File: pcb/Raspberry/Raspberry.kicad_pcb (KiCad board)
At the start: 2 copper layers, 66.4 x 48.1 mm, 26 parts, among them J1 +5V, J10 SWCLK, J11 GND, J12 SWDIO, J13 UART_TX, J14 UART_RX, J15 PC1, J16 PC0, J17 PB14, J18 GND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

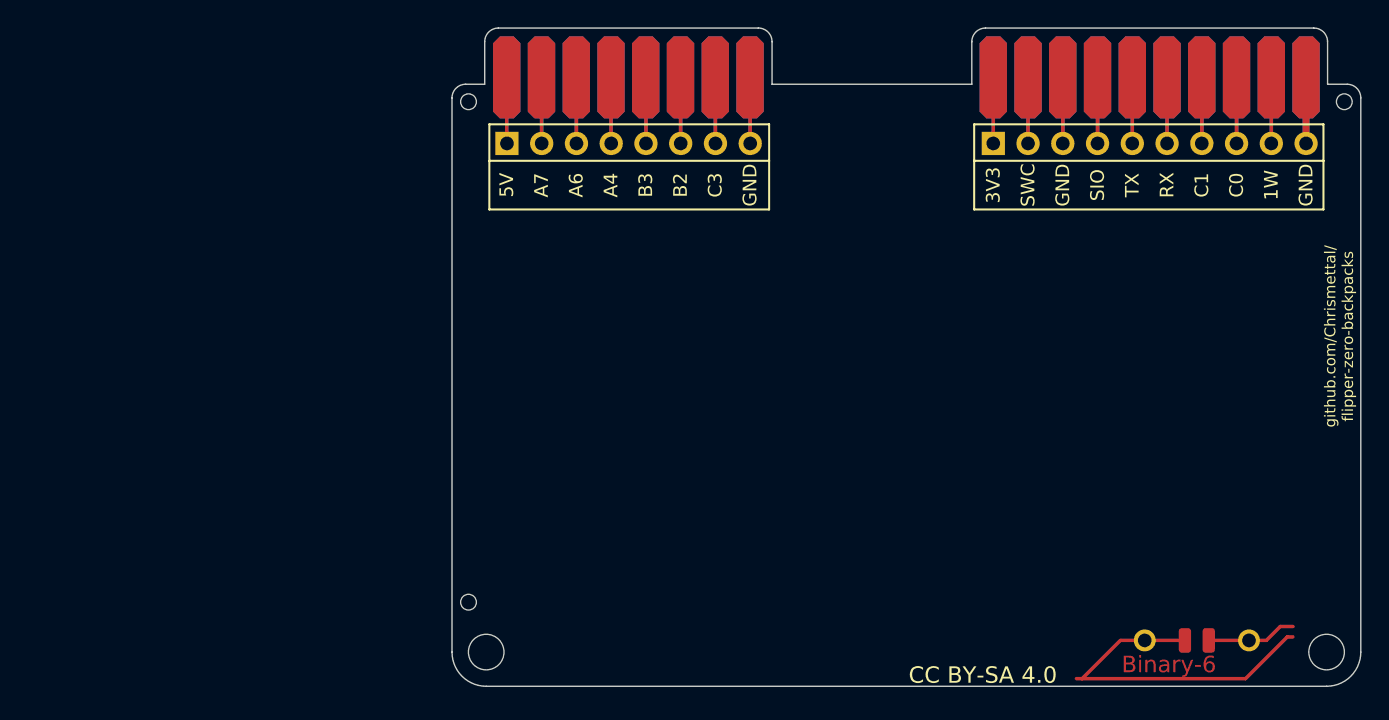
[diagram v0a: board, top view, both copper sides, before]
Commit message: [RPI] Draw schematic
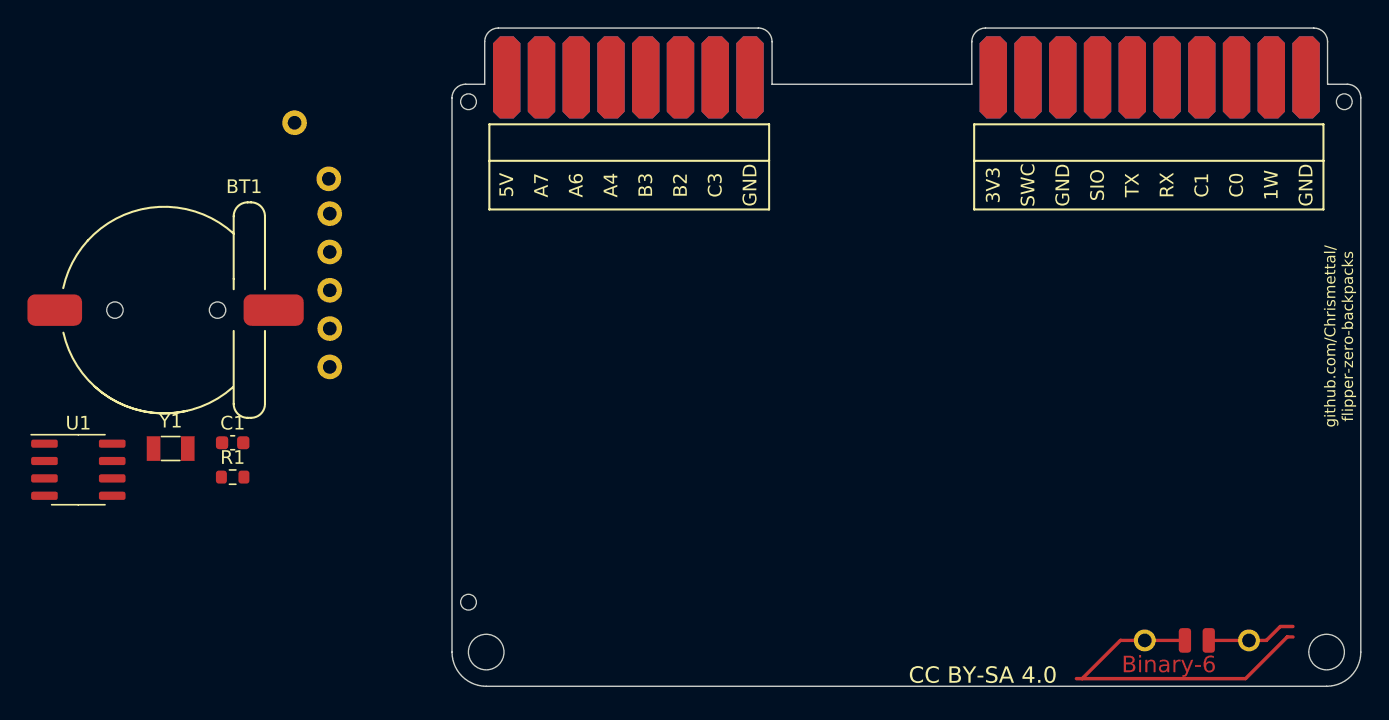
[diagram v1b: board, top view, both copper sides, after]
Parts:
- added BT1: CR1220, MeineBib:Q&J CR1220-2, F.Cu at (78.5, 104.2)
- added C1: 2.2µF, Capacitor_SMD:C_0603_1608Metric, F.Cu at (83.5, 113.9)
- added J19: +5V, MeineBib:Protopin_Small, F.Cu at (90.6, 97.1)
- added J22: FplRX_RpiTX, MeineBib:Protopin_Small, F.Cu at (90.6, 99.9)
- added J23: FlpTX_RpiRX, MeineBib:Protopin_Small, F.Cu at (90.6, 102.7)
- added J24: SCL, MeineBib:Protopin_Small, F.Cu at (90.6, 105.5)
- added J25: SDA, MeineBib:Protopin_Small, F.Cu at (90.6, 108.3)
- added R1: 1K, Resistor_SMD:R_0603_1608Metric, F.Cu at (83.5, 116.4)
- added U1: PCF8523T, Package_SO:SOIC-8_3.9x4.9mm_P1.27mm, F.Cu at (72.2, 115.9)
- added Y1: 32.768kHz, Crystal:Crystal_SMD_3215-2Pin_3.2x1.5mm, F.Cu at (78.9, 114.3)
- J20: value Conn_01x10 -> +3V3; footprint Connector_PinHeader_2.54mm:PinHeader_1x10_P2.54mm_Vertical -> MeineBib:Protopin_Small
- J21: value Conn_01x08 -> Gnd; footprint Connector_PinHeader_2.54mm:PinHeader_1x08_P2.54mm_Vertical -> MeineBib:Protopin_Small
- moved J20 48.6 mm to (90.5, 94.6)
- moved J21 15.6 mm to (88.0, 90.5)
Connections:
- J1 pad 1: Ext_+5V -> Net-(J1-Pin_1)
- J10 pad 1: Net-(J10-Pin_1) -> unconnected-(J10-Pin_1-Pad1)
- J11 pad 1: GND -> unconnected-(J11-Pin_1-Pad1)
- J12 pad 1: Net-(J12-Pin_1) -> unconnected-(J12-Pin_1-Pad1)
- J15 pad 1: Net-(J15-Pin_1) -> unconnected-(J15-Pin_1-Pad1)
- J16 pad 1: Net-(J16-Pin_1) -> unconnected-(J16-Pin_1-Pad1)
- J17 pad 1: Net-(J17-Pin_1) -> unconnected-(J17-Pin_1-Pad1)
- J2 pad 1: Net-(J2-Pin_1) -> unconnected-(J2-Pin_1-Pad1)
- J20 pad 1: Ext_+3.3V -> Net-(J20-Pin_1)
- J21 pad 1: Ext_+5V -> GND
- J3 pad 1: Net-(J21-Pin_3) -> unconnected-(J3-Pin_1-Pad1)
- J4 pad 1: Net-(J21-Pin_4) -> unconnected-(J4-Pin_1-Pad1)
- J5 pad 1: Net-(J21-Pin_5) -> unconnected-(J5-Pin_1-Pad1)
- J6 pad 1: Net-(J21-Pin_6) -> unconnected-(J6-Pin_1-Pad1)
- J7 pad 1: Net-(J21-Pin_7) -> unconnected-(J7-Pin_1-Pad1)
- J8 pad 1: GND -> unconnected-(J8-Pin_1-Pad1)
- J9 pad 1: Ext_+3.3V -> unconnected-(J9-Pin_1-Pad1)
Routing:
- net GND: track 29.0 -> 0.00 mm
- net Net-(J21-Pin_7): track 9.66 -> 0.00 mm
- net Net-(J17-Pin_1): track 9.65 -> 0.00 mm
- net Net-(J16-Pin_1): track 9.65 -> 0.00 mm
- net Net-(J15-Pin_1): track 9.65 -> 0.00 mm
- net Net-(J14-Pin_1): track 9.65 -> 0.00 mm
- net Net-(J13-Pin_1): track 9.65 -> 0.00 mm
- net Net-(J12-Pin_1): track 9.65 -> 0.00 mm
- net Net-(J10-Pin_1): track 9.65 -> 0.00 mm
- net Ext_+3.3V: track 9.65 -> 0.00 mm
- net Net-(J21-Pin_6): track 9.64 -> 0.00 mm
- net Net-(J21-Pin_5): track 9.64 -> 0.00 mm
- net Net-(J21-Pin_4): track 9.64 -> 0.00 mm
- net Net-(J21-Pin_3): track 9.64 -> 0.00 mm
- net Net-(J2-Pin_1): track 9.64 -> 0.00 mm
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
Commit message: [RPI] Route PCB
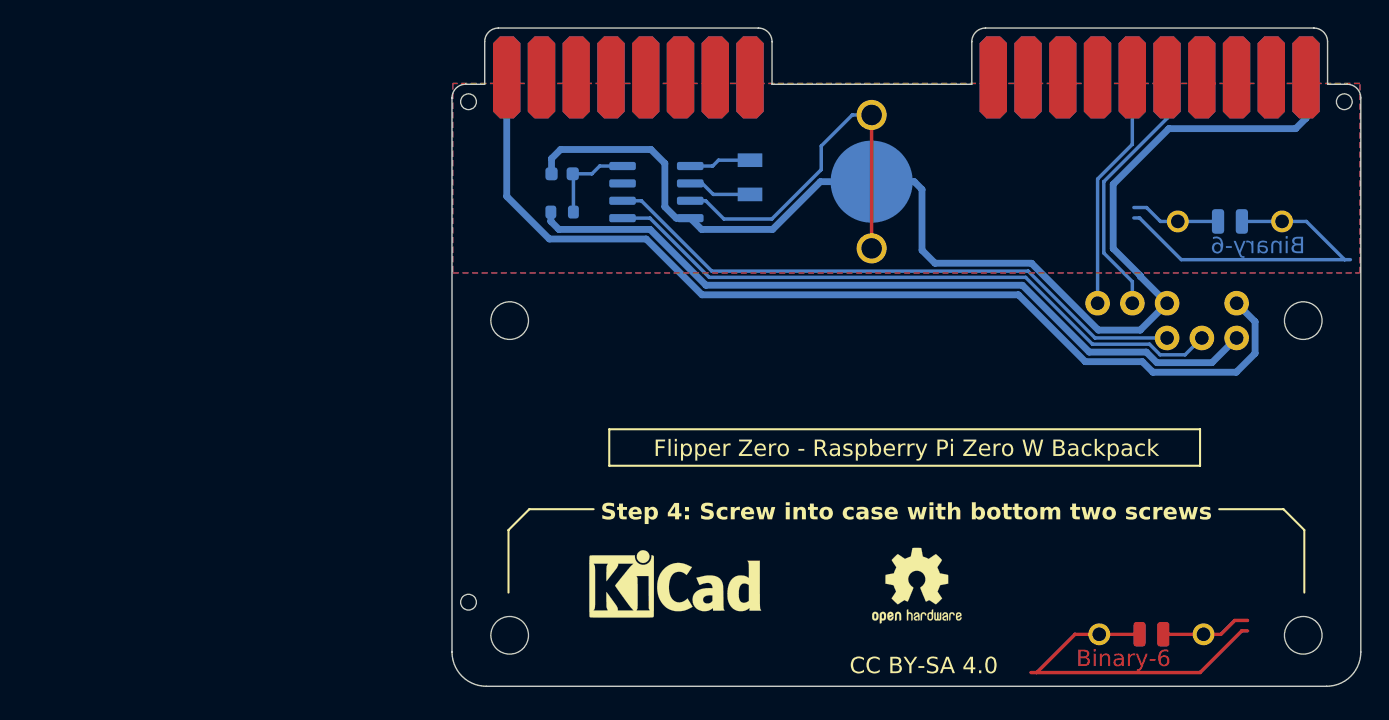
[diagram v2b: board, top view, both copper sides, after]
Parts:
- removed MK2 (x2): Mounting_Hole, MeineBib:EigenesMountingHole_2.6mm_M2.5_Small
- added H7: Symbol_Binary6, MeineBib:Binary_6_v0.1_tiny_silk, B.Cu at (156.3, 98.7)
- added REF**: Raspberry_Pi_Zero_Socketed_THT_FaceDown_MountingHoles, Module:Raspberry_Pi_Zero_Socketed_THT_FaceDown_MountingHoles, F.Cu at (156.8, 106.2)
- added REF**: OSHW-Logo2_7.3x6mm_SilkScreen, Symbol:OSHW-Logo2_7.3x6mm_SilkScreen, F.Cu at (133.5, 124.3)
- added REF**: KiCad-Logo_5mm_SilkScreen, Symbol:KiCad-Logo_5mm_SilkScreen, F.Cu at (115.8, 124.7)
- BT1: value CR1220 -> CR927 (3V); footprint MeineBib:Q&J CR1220-2 -> MeineBib:MY-927-01 CR927 Battery Holder; moved to B.Cu
- C1, R1, U1, Y1: moved to B.Cu
- moved J20 67.4 mm to (156.8, 106.2)
- moved J19 66.6 mm to (156.8, 103.7)
- moved J21 65.1 mm to (151.8, 103.7)
- moved J25 63.8 mm to (154.3, 106.2)
- moved J24 61.2 mm to (151.8, 106.2)
- moved J22 58.8 mm to (149.2, 103.7)
- moved J23 56.1 mm to (146.7, 103.7)
- moved BT1 52.6 mm to (130.2, 94.8), turned to -90 degrees
- moved U1 46.9 mm to (114.4, 95.6), turned to 180 degrees
- moved Y1 46.8 mm to (121.3, 94.5), turned to 90 degrees
- moved C1 31.1 mm to (107.6, 94.2), turned to 180 degrees
- moved R1 30.9 mm to (107.6, 97.0)
- moved H7 3.35 mm to (150.6, 128.9)
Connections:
- net Net-(J1-Pin_1) renamed +5V
- net Net-(J13-Pin_1) renamed /FlpTX_RpiRX
- net Net-(J14-Pin_1) renamed /FlpRX_RpiTX
- net Net-(J20-Pin_1) renamed +3V3
- net Net-(J24-Pin_1) renamed /SCL
- net Net-(J25-Pin_1) renamed /SDA
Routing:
- net GND: track 0.00 -> 89.4 mm
- net +5V: track 0.00 -> 73.5 mm
- net +3V3: track 0.00 -> 55.8 mm
- net /SDA: track 0.00 -> 47.0 mm
- net /SCL: track 0.00 -> 44.0 mm
- net Net-(BT1-+): track 0.00 -> 27.7 mm
- net /FlpRX_RpiTX: track 0.00 -> 19.3 mm
- net /FlpTX_RpiRX: track 0.00 -> 17.6 mm
- net Net-(U1-VDD): track 0.00 -> 6.69 mm
- net Net-(U1-OSCO): track 0.00 -> 4.70 mm
- net Net-(U1-OSCI): track 0.00 -> 4.54 mm
- added copper zone on B.Cu, net (none)
- added copper zone on F.Cu, net (none)
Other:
- board text added: "(Screw from below, nuts on top of Rpi)"
- board text added: "CR927 (3V)"
- board text added: "Flipper Zero - Raspberry Pi Zero W Backpack"
- board text added: "SD"
- board text added: "Step 1: Place RPI here"
- board text added: "Step 2: Screw on with top 2 screws"
- board text added: "Step 3: Solder from both sides"
- board text added: "Step 4: Screw into case with bottom two screws"
- board text added: "USB"
- board text removed: "1W"
- board text removed: "3V3"
- board text removed: "5V"
- board text removed: "A4"
- board text removed: "A6"
- board text removed: "A7"
- board text removed: "B2"
- board text removed: "B3"
- board text removed: "C0"
- board text removed: "C1"
- board text removed: "C3"
- board text removed: "GND"
- board text removed: "RX"
- board text removed: "SIO"
- board text removed: "SWC"
- board text removed: "TX"

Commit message: [RPI] Export fabrication files
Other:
- board text added: "925b344"
- board text added: "JLCJLCJLCJLC"
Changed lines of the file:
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@@
     (effects (font (size 1.2 1.2) (thickness 0.2) bold) (justify left bottom mirror))
+  )
+  (gr_text "JLCJLCJLCJLC" (at 154.686 131.191) (layer "B.SilkS")
+    (effects (font (size 0.8 0.8) (thickness 0.12)) (justify left bottom mirror))
   )
   (gr_text "USB" (at 126.873 131.318) (layer "B.SilkS")
@@
     (effects (font (size 1.2 1.2) (thickness 0.2)))
   )
+  (gr_text "925b344" (at 113.665 130.937) (layer "F.SilkS")
+    (effects (font (size 0.8 0.8) (thickness 0.12)) (justify left bottom))
+  )
   (gr_text "Flipper Zero - Raspberry Pi Zero W Backpack" (at 132.715 114.3) (layer "F.SilkS")

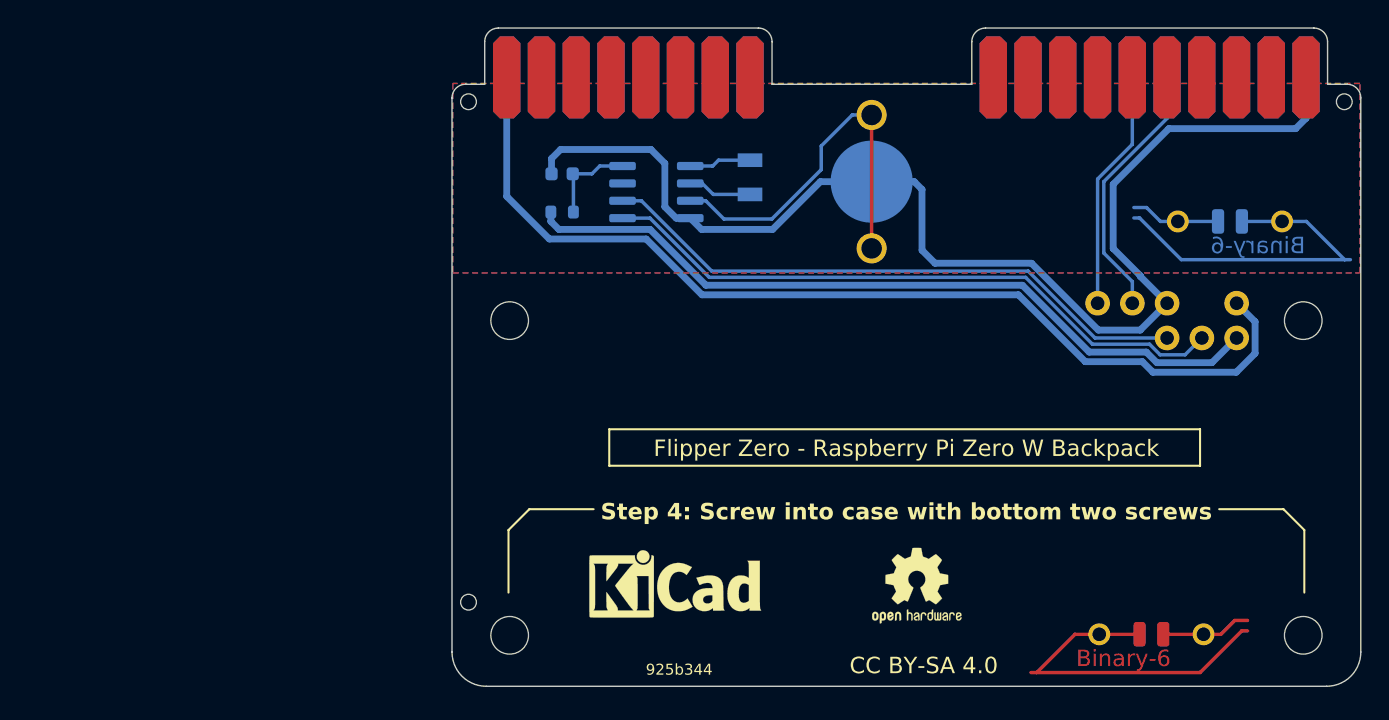
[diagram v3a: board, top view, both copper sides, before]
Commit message: [RPI] Fix PCB not actually connected to Flipper
- Added previously removed headers that act as mandatory vias from one side to the other.
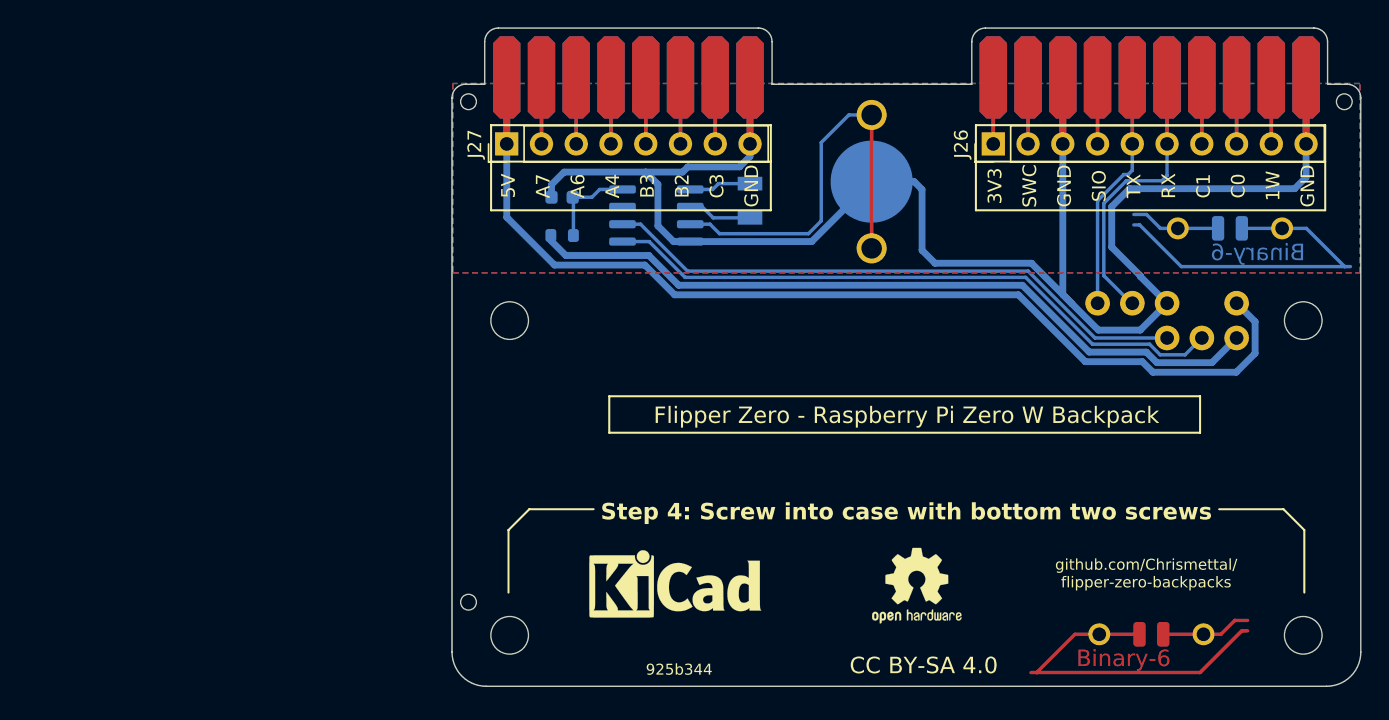
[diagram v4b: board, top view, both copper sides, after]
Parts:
- added J26: Conn_01x10, Connector_PinHeader_2.54mm:PinHeader_1x10_P2.54mm_Vertical, F.Cu at (139.1, 92.0)
- added J27: Conn_01x08, Connector_PinHeader_2.54mm:PinHeader_1x08_P2.54mm_Vertical, F.Cu at (103.5, 92.0)
- moved C1 1.71 mm to (107.6, 95.9)
- moved R1 1.71 mm to (107.6, 98.7)
- moved U1 1.71 mm to (114.4, 97.3)
- moved Y1 1.71 mm to (121.3, 96.2)
- moved H7 0.51 mm to (156.3, 99.2)
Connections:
- J10 pad 1: unconnected-(J10-Pin_1-Pad1) -> Net-(J10-Pin_1)
- J11 pad 1: unconnected-(J11-Pin_1-Pad1) -> GND
- J12 pad 1: unconnected-(J12-Pin_1-Pad1) -> Net-(J12-Pin_1)
- J15 pad 1: unconnected-(J15-Pin_1-Pad1) -> Net-(J15-Pin_1)
- J16 pad 1: unconnected-(J16-Pin_1-Pad1) -> Net-(J16-Pin_1)
- J17 pad 1: unconnected-(J17-Pin_1-Pad1) -> Net-(J17-Pin_1)
- J2 pad 1: unconnected-(J2-Pin_1-Pad1) -> Net-(J2-Pin_1)
- J3 pad 1: unconnected-(J3-Pin_1-Pad1) -> Net-(J27-Pin_3)
- J4 pad 1: unconnected-(J4-Pin_1-Pad1) -> Net-(J27-Pin_4)
- J5 pad 1: unconnected-(J5-Pin_1-Pad1) -> Net-(J27-Pin_5)
- J6 pad 1: unconnected-(J6-Pin_1-Pad1) -> Net-(J27-Pin_6)
- J7 pad 1: unconnected-(J7-Pin_1-Pad1) -> Net-(J27-Pin_7)
- J8 pad 1: unconnected-(J8-Pin_1-Pad1) -> GND
- J9 pad 1: unconnected-(J9-Pin_1-Pad1) -> Net-(J26-Pin_1)
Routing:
- net GND: track 89.4 -> 136.3 mm
- net Net-(J27-Pin_7): track 0.00 -> 9.72 mm
- net Net-(J27-Pin_6): track 0.00 -> 9.72 mm
- net Net-(J27-Pin_5): track 0.00 -> 9.72 mm
- net Net-(J27-Pin_4): track 0.00 -> 9.72 mm
- net Net-(J27-Pin_3): track 0.00 -> 9.72 mm
- net Net-(J26-Pin_1): track 0.00 -> 9.72 mm
- net Net-(J2-Pin_1): track 0.00 -> 9.72 mm
- net Net-(J17-Pin_1): track 0.00 -> 9.72 mm
- net Net-(J16-Pin_1): track 0.00 -> 9.72 mm
- net Net-(J15-Pin_1): track 0.00 -> 9.72 mm
- net Net-(J12-Pin_1): track 0.00 -> 9.72 mm
- net Net-(J10-Pin_1): track 0.00 -> 9.72 mm
- net /FlpRX_RpiTX: track 19.3 -> 25.7 mm
- net +5V: track 73.5 -> 79.3 mm
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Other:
- board text added: "1W"
- board text added: "3V3"
- board text added: "5V"
- board text added: "A4"
- board text added: "A6"
- board text added: "A7"
- board text added: "B2"
- board text added: "B3"
- board text added: "C0"
- board text added: "C1"
- board text added: "C3"
- board text added: "GND"
- board text added: "RX"
- board text added: "SIO"
- board text added: "SWC"
- board text added: "TX"

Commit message: [RPI] Order boards
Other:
- board text added: "41a3985"
- board text removed: "925b344"
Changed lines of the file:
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@@
     (effects (font (size 1 1) (thickness 0.2)) (justify mirror))
   )
-  (gr_text "github.com/Chrismettal/\nflipper-zero-backpacks" (at 119.38 100.203) (layer "B.SilkS")
+  (gr_text "github.com/Chrismettal/\nflipper-zero-backpacks" (at 142.621 100.076) (layer "B.SilkS")
     (effects (font (size 0.8 0.8) (thickness 0.12)) (justify mirror))
   )
@@
     (effects (font (size 1 1) (thickness 0.2)))
   )
-  (gr_text "925b344" (at 113.665 130.937) (layer "F.SilkS")
+  (gr_text "41a3985" (at 113.665 130.937) (layer "F.SilkS")
     (effects (font (size 0.8 0.8) (thickness 0.12)) (justify left bottom))
   )

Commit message: Remove JLCJLCJLCJLC String from all PCBs
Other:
- board text removed: "JLCJLCJLCJLC"
